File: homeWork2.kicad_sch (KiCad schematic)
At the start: 44 parts, among them J1 Barrel_Jack_Switch_SMT, U1 LM7805_TO220

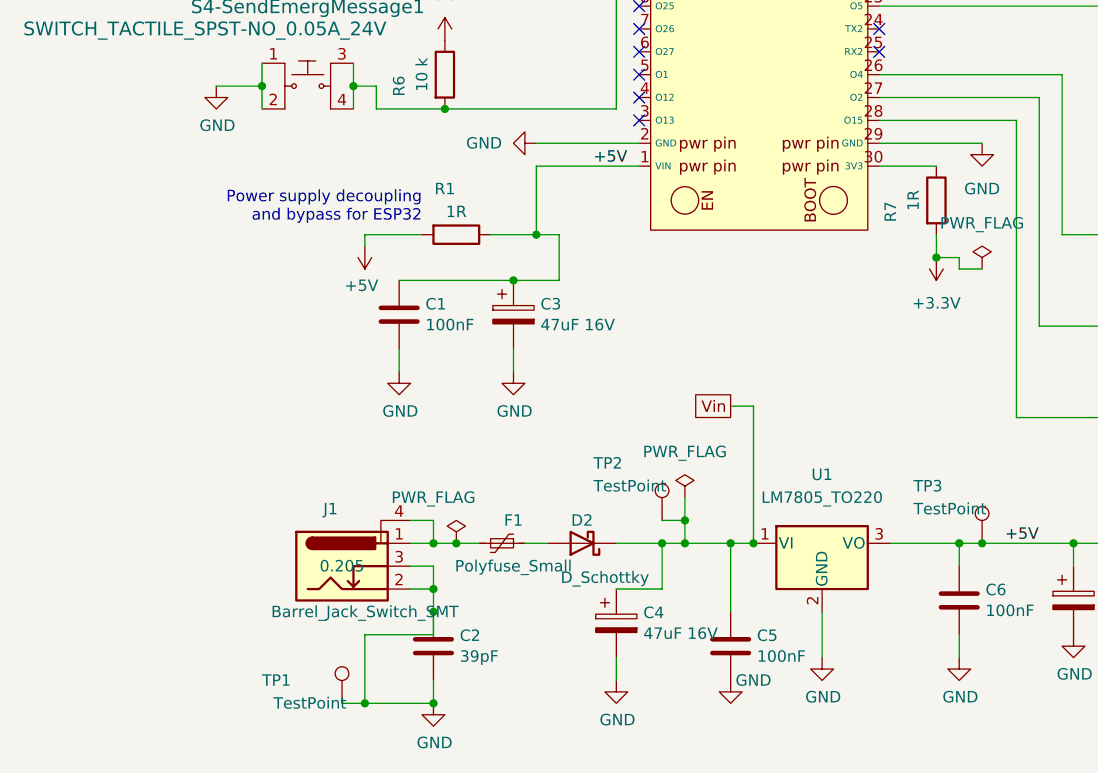
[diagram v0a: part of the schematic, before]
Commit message: capacitors are placed for high frequency and to minimize stray conductance. Classes are editted and a unique Net class is added for power and some net are renamed and assigned to it the suitable Net Class. For example, Vin PVRAW ESP1-3V3 and ESP1-5V are assgined to it PWR Net class.
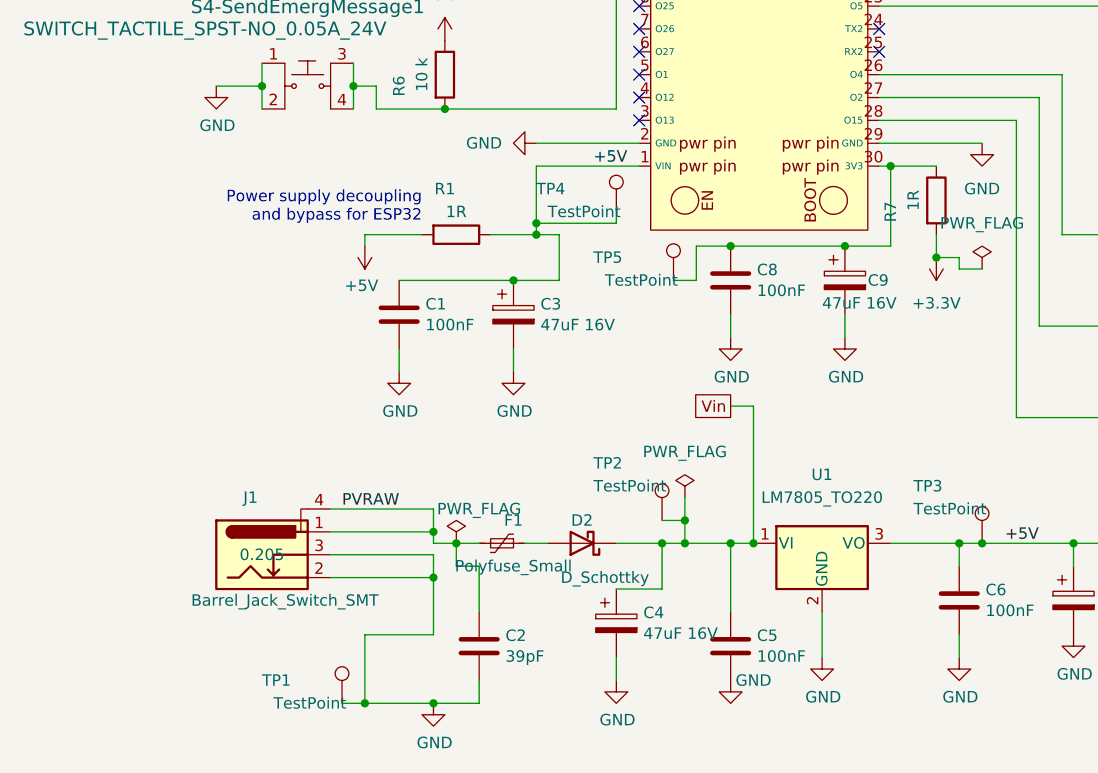
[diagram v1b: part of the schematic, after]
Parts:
- added C8: 100nF, Capacitor_SMD:C_0603_1608Metric_Pad1.08x0.95mm_HandSolder, symbol Device:C
- added C9: 47uF 16V, Capacitor_SMD:CP_Elec_5x5.4, symbol Device:C_Polarized
- added TP4, TP5: TestPoint, TestPoint:TestPoint_Loop_D2.54mm_Drill1.5mm_Beaded, symbol Connector:TestPoint
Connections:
- net +5V: now also TP4.1
- net GND: now also C8.2, C9.2; no longer C2.1
- net at ESP1.30 (3V3), R7.1: now also C8.1, C9.1, TP5.1
- net PVRAW: now reaches F1.2, J1.1, J1.4
- net PVRAW: now also C2.1
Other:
- moved on the sheet: C2, J1

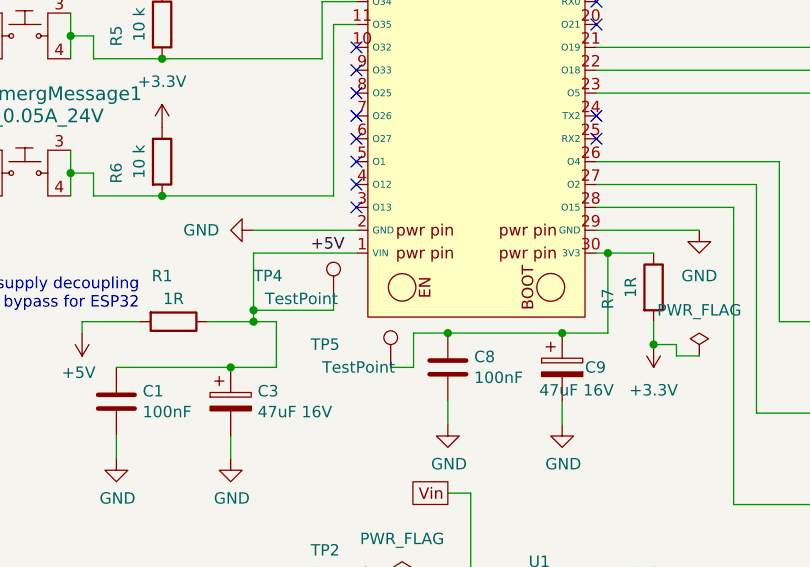
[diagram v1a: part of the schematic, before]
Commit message: changing net names to better use the net classes. Corrected a short across resistor R1.
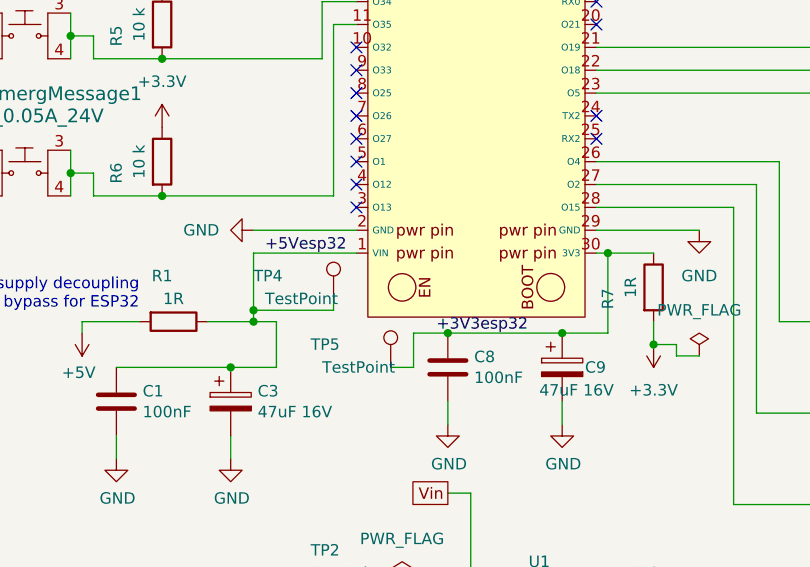
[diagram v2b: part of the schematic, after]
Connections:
- net +5V: no longer C1.1, C3.1, ESP1.1 (VIN), R1.1, TP4.1
- net +3V3esp32: now reaches C8.1, C9.1, ESP1.30 (3V3), R7.1, TP5.1
- new net +5Vesp32: C1.1, C3.1, ESP1.1 (VIN), R1.1, TP4.1
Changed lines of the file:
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@@
     (effects (font (size 1.27 1.27)) (justify left bottom))
   )
-  (label "+5V" (at 93.98 116.84 0) (fields_autoplaced)
+  (label "+5Vesp32" (at 88.9 116.84 0) (fields_autoplaced)
     (effects (font (size 1.27 1.27)) (justify left bottom))
   )
+  (label "+3V3esp32" (at 107.95 125.73 0) (fields_autoplaced)
+    (effects (font (size 1.27 1.27)) (justify left bottom))
+  )

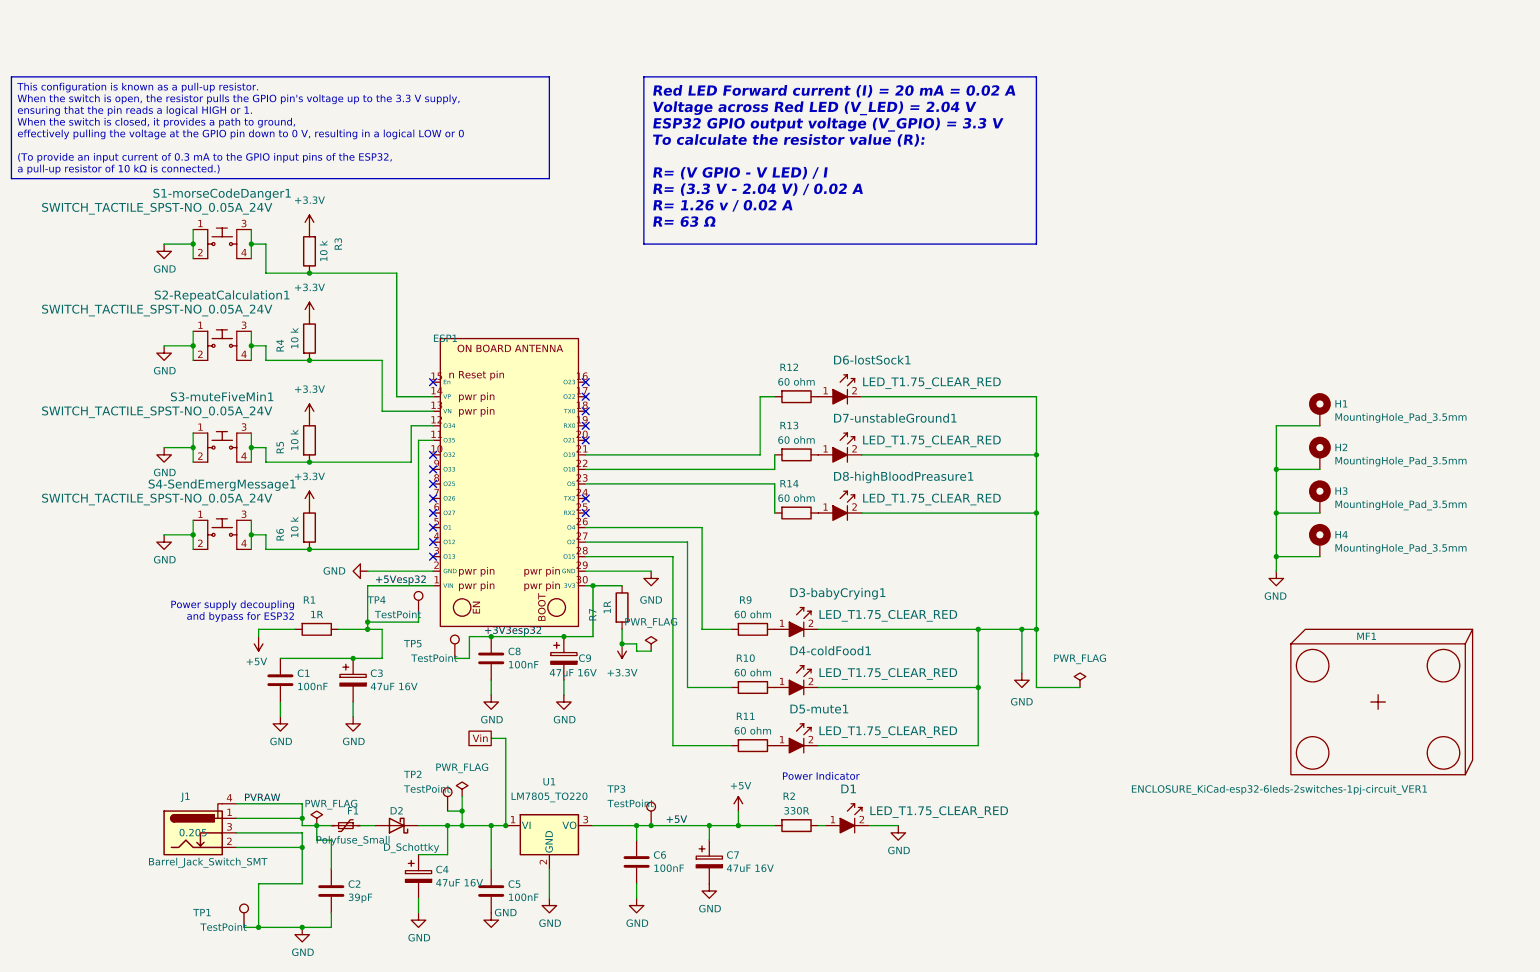
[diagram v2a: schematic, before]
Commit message: Edited the ESP32 footprint. Rerouted the PCBa and added female socket connectors to the ESP32 and two others to connect an LCD and a DFPLAYER
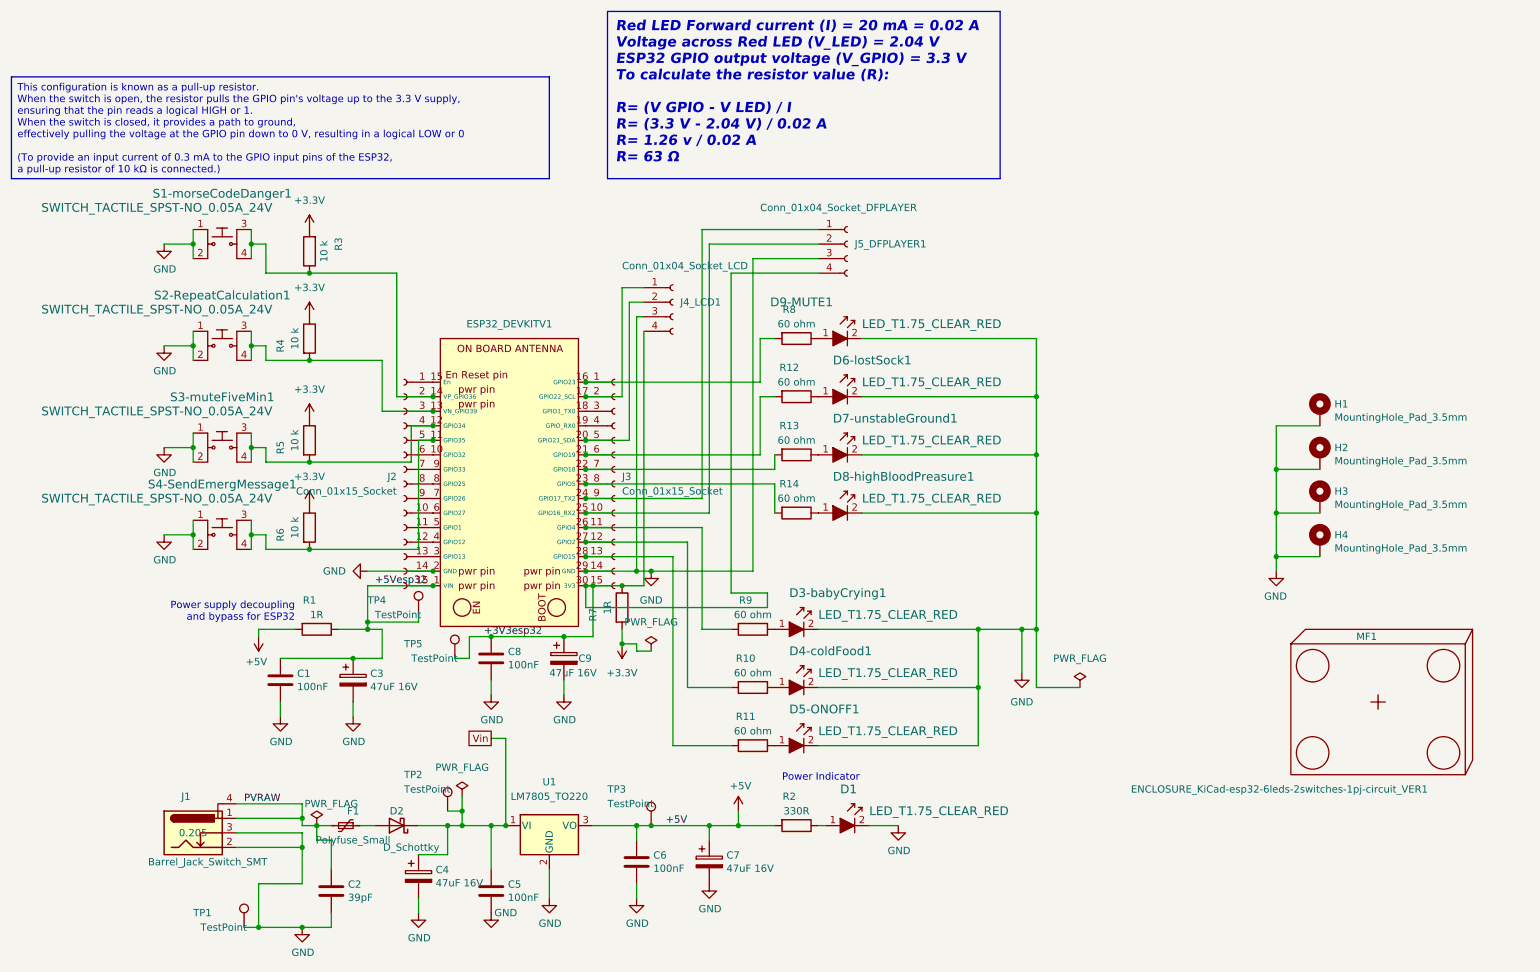
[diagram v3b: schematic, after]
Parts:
- added D9-MUTE1: LED_T1.75_CLEAR_RED, PubInv_KiCad_PCB:LED_5mm_Radial, symbol GPAD_SCH_LIB:LED_T1.75_CLEAR_WHITE
- added J2, J3: Conn_01x15_Socket, Connector_PinSocket_2.54mm:PinSocket_1x15_P2.54mm_Vertical, symbol Connector:Conn_01x15_Socket
- added J4_LCD1: Conn_01x04_Socket_LCD, Connector_PinSocket_2.54mm:PinSocket_1x04_P2.54mm_Vertical, symbol Connector:Conn_01x04_Socket
- added J5_DFPLAYER1: Conn_01x04_Socket_DFPLAYER, Connector_PinSocket_2.54mm:PinSocket_1x04_P2.54mm_Vertical, symbol Connector:Conn_01x04_Socket
- added R8: 60 ohm, Resistor_SMD:R_0603_1608Metric_Pad0.98x0.95mm_HandSolder, symbol Device:R
- ESP32_DEVKITV1: renamed from ESP1; footprint esp32 15 pin Library:esp32 -> PubInv_KiCad_PCB:ESP32_DEVKITV1; symbol New_Library.ESP32KIT:ESP32_-_V2 -> PubInv_KiCad_SCH_LIB:ESP32_DEVKITV1
- renumbered D5-mute1 to D5-ONOFF1
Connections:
- net +3V3esp32: now also J3.15 (Pin_15), J4_LCD1.4 (Pin_4), J5_DFPLAYER1.4 (Pin_4)
- net +5Vesp32: now also J2.15 (Pin_15)
- net GND: now also D9-MUTE1.2, J2.14 (Pin_14), J3.14 (Pin_14), J4_LCD1.3 (Pin_3), J5_DFPLAYER1.3 (Pin_3)
- net at ESP32_DEVKITV1.27 (GPIO2), R10.2: now also J3.12 (Pin_12)
- net at ESP32_DEVKITV1.10 (GPIO32): now also J2.6 (Pin_6)
- net at ESP32_DEVKITV1.11 (GPIO35), R6.2, S4-SendEmergMessage1.3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: now also J2.5 (Pin_5)
- net at ESP32_DEVKITV1.12 (GPIO34), R5.2, S3-muteFiveMin1.3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: now also J2.4 (Pin_4)
- net at ESP32_DEVKITV1.13 (VN_GPIO39), R4.2, S2-RepeatCalculation1.3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: now also J2.3 (Pin_3)
- net at ESP32_DEVKITV1.14 (VP_GPIO36), R3.1, S1-morseCodeDanger1.3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: now also J2.2 (Pin_2)
- net at ESP32_DEVKITV1.15 (En): now also J2.1 (Pin_1)
- net at ESP32_DEVKITV1.16 (GPIO23): now also J3.1 (Pin_1), R8.2
- net at ESP32_DEVKITV1.17 (GPIO22_SCL): now also J3.2 (Pin_2), J4_LCD1.1 (Pin_1)
- net at ESP32_DEVKITV1.18 (GPIO1_TX0): now also J3.3 (Pin_3)
- net at ESP32_DEVKITV1.19 (GPIO_RX0): now also J3.4 (Pin_4)
- net at ESP32_DEVKITV1.20 (GPIO21_SDA): now also J3.5 (Pin_5), J4_LCD1.2 (Pin_2)
- net at ESP32_DEVKITV1.21 (GPIO19), R12.2: now also J3.6 (Pin_6)
- net at ESP32_DEVKITV1.22 (GPIO18), R13.2: now also J3.7 (Pin_7)
- net at ESP32_DEVKITV1.23 (GPIO5), R14.2: now also J3.8 (Pin_8)
- net at ESP32_DEVKITV1.24 (GPIO17_TX2): now also J3.9 (Pin_9), J5_DFPLAYER1.1 (Pin_1)
- net at ESP32_DEVKITV1.25 (GPIO16_RX2): now also J3.10 (Pin_10), J5_DFPLAYER1.2 (Pin_2)
- net at ESP32_DEVKITV1.26 (GPIO4), R9.2: now also J3.11 (Pin_11)
- net at ESP32_DEVKITV1.28 (GPIO15), R11.2: now also J3.13 (Pin_13)
- net at ESP32_DEVKITV1.3 (GPIO13): now also J2.13 (Pin_13)
- net at ESP32_DEVKITV1.4 (GPIO12): now also J2.12 (Pin_12)
- net at ESP32_DEVKITV1.5 (GPIO1): now also J2.11 (Pin_11)
- net at ESP32_DEVKITV1.6 (GPIO27): now also J2.10 (Pin_10)
- net at ESP32_DEVKITV1.7 (GPIO26): now also J2.9 (Pin_9)
- net at ESP32_DEVKITV1.8 (GPIO25): now also J2.8 (Pin_8)
- net at ESP32_DEVKITV1.9 (GPIO33): now also J2.7 (Pin_7)
- new net: D9-MUTE1.1, R8.1
- no-connect marks 16 -> 0
